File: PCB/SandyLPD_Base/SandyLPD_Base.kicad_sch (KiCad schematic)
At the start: 234 parts, among them J1 Conn_02x02_Odd_Even, J10 Conn_01x10_Pin, J11 Conn_01x03, J12 Conn_01x01_Pin, J2 Conn_01x03, J3 Conn_01x01_Pin, J4 Conn_01x10_Pin, J5 USB_C_Receptacle_USB2.0, J6 USB_C_Receptacle_USB2.0, J7 USB_C_Receptacle_USB2.0, J8 USB_C_Receptacle_USB2.0, J9 Conn_02x02_Odd_Even, SW1 BOOT_ALT, SW2 RESET_ALT, SW3 SW_DIP_x04, SW4 BOOT_ALT, SW5 RESET_ALT, SW6 SW_DIP_x04, U1 NCP1117-3.3_SOT223, U2 NCP1117-3.3_SOT223, U3 RP2040, U4 W25Q128JVPIQ, U5 RP2040, U6 W25Q128JVPIQ, Y1 12MHz, Y2 12MHz

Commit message: フラッシュメモリの部品置き換わりを修正
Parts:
- U4, U6: footprint Package_SO:SOIC-8_5.23x5.23mm_P1.27mm -> Package_SON:WSON-8-1EP_6x5mm_P1.27mm_EP3.4x4.3mm; symbol Memory_Flash:W25Q128JVS -> Memory_Flash:W25Q128JVP
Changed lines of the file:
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@@
 			)
 		)
-		(symbol "Memory_Flash:W25Q128JVS"
+		(symbol "Memory_Flash:W25Q128JVP"
 			(exclude_from_sim no)
 			(in_bom yes)
@@
 				)
 			)
-			(property "Value" "W25Q128JVS"
+			(property "Value" "W25Q128JVP"
 				(at 7.62 11.43 0)
 				(effects
@@
 				)
 			)
-			(property "Footprint" "Package_SO:SOIC-8_5.23x5.23mm_P1.27mm"
+			(property "Footprint" "Package_SON:WSON-8-1EP_6x5mm_P1.27mm_EP3.4x4.3mm"
 				(at 0 22.86 0)
 				(effects
@@
 				)
 			)
-			(property "Description" "128Mb Serial Flash Memory, Standard/Dual/Quad SPI, SOIC-8"
+			(property "Description" "128Mb Serial Flash Memory, Standard/Dual/Quad SPI, WSON-8"
 				(at 0 27.94 0)
 				(effects
@@
 				)
 			)
-			(property "ki_keywords" "flash memory SPI QPI DTR"
+			(property "ki_keywords" "flash memory SPI"
 				(at 0 0 0)
 				(effects
@@
 				)
 			)
-			(property "ki_fp_filters" "SOIC*5.23x5.23mm*P1.27mm*"
+			(property "ki_fp_filters" "WSON*1EP*6x5mm*P1.27mm*EP3.4x4.3mm*"
 				(at 0 0 0)
 				(effects
@@
 				)
 			)
-			(symbol "W25Q128JVS_0_1"
+			(symbol "W25Q128JVP_0_1"
 				(rectangle
 					(start -7.62 10.16)
@@
 				)
 			)
-			(symbol "W25Q128JVS_1_1"
+			(symbol "W25Q128JVP_1_1"
 				(pin input line
 					(at -10.16 7.62 0)
@@
 	)
 	(symbol
-		(lib_id "Memory_Flash:W25Q128JVS")
+		(lib_id "Memory_Flash:W25Q128JVP")
 		(at 305.435 144.78 0)
 		(unit 1)
@@
 			)
 		)
-		(property "Footprint" "Package_SO:SOIC-8_5.23x5.23mm_P1.27mm"
-			(at 305.435 144.78 0)
+		(property "Footprint" "Package_SON:WSON-8-1EP_6x5mm_P1.27mm_EP3.4x4.3mm"
+			(at 305.435 121.92 0)
 			(effects
 				(font
@@
 		)
 		(property "Datasheet" "https://www.winbond.com/resource-files/w25q128jv_dtr%20revc%2003272018%20plus.pdf"
-			(at 305.435 144.78 0)
+			(at 305.435 119.38 0)
 			(effects
 				(font
@@
 			)
 		)
-		(property "Description" "128Mb Serial Flash Memory, Standard/Dual/Quad SPI, SOIC-8"
-			(at 305.435 144.78 0)
+		(property "Description" "128Mb Serial Flash Memory, Standard/Dual/Quad SPI, WSON-8"
+			(at 305.435 116.84 0)
 			(effects
 				(font
@@
 	)
 	(symbol
-		(lib_id "Memory_Flash:W25Q128JVS")
+		(lib_id "Memory_Flash:W25Q128JVP")
 		(at 577.215 144.78 0)
 		(unit 1)
@@
 			)
 		)
-		(property "Footprint" "Package_SO:SOIC-8_5.23x5.23mm_P1.27mm"
-			(at 577.215 144.78 0)
+		(property "Footprint" "Package_SON:WSON-8-1EP_6x5mm_P1.27mm_EP3.4x4.3mm"
+			(at 577.215 121.92 0)
 			(effects
 				(font
@@
 		)
 		(property "Datasheet" "https://www.winbond.com/resource-files/w25q128jv_dtr%20revc%2003272018%20plus.pdf"
-			(at 577.215 144.78 0)
+			(at 577.215 119.38 0)
 			(effects
 				(font
@@
 			)
 		)
-		(property "Description" "128Mb Serial Flash Memory, Standard/Dual/Quad SPI, SOIC-8"
-			(at 577.215 144.78 0)
+		(property "Description" "128Mb Serial Flash Memory, Standard/Dual/Quad SPI, WSON-8"
+			(at 577.215 116.84 0)
 			(effects
 				(font

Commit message: 仮配線中
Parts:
- removed J3: Conn_01x01_Pin, TestPoint:TestPoint_THTPad_D1.0mm_Drill0.5mm, symbol Connector:Conn_01x01_Pin
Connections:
- net L_RESERVE1: now also J4.1 (Pin_1), U3.5 (GPIO3); no longer J4.3 (Pin_3), U3.4 (GPIO2)
- net L_RESERVE2: now also J4.2 (Pin_2), U3.6 (GPIO4); no longer J4.4 (Pin_4), U3.5 (GPIO3)
- net L_RESERVE3: now also J4.3 (Pin_3), U3.7 (GPIO5); no longer J4.5 (Pin_5), U3.6 (GPIO4)
- net L_RESERVE4: now also J4.4 (Pin_4), U3.8 (GPIO6); no longer J4.6 (Pin_6), U3.7 (GPIO5)
- net L_RESERVE5: now also J4.5 (Pin_5), U3.9 (GPIO7); no longer J4.7 (Pin_7), U3.8 (GPIO6)
- net L_RESERVE6: now also J4.7 (Pin_7), U3.11 (GPIO8); no longer J4.8 (Pin_8), U3.9 (GPIO7)
- net L_RESERVE7: now also J4.8 (Pin_8), U3.12 (GPIO9); no longer J4.9 (Pin_9), U3.11 (GPIO8)
- net L_RESERVE8: now also J4.9 (Pin_9), U3.13 (GPIO10); no longer J4.10 (Pin_10), U3.12 (GPIO9)
- net L_RESERVE9: now also J4.10 (Pin_10), U3.14 (GPIO11); no longer U3.13 (GPIO10)
- net L_col5: now also U3.4 (GPIO2); no longer U3.18 (GPIO15)
- net L_dip1: now also U3.15 (GPIO12); no longer U3.14 (GPIO11)
- net L_dip2: now also U3.16 (GPIO13); no longer U3.15 (GPIO12)
- net L_dip3: now also U3.17 (GPIO14); no longer U3.16 (GPIO13)
- net L_dip4: now also U3.18 (GPIO15); no longer U3.17 (GPIO14)
- no-connect marks 30 -> 29
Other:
- moved on the sheet: SW3, SW6

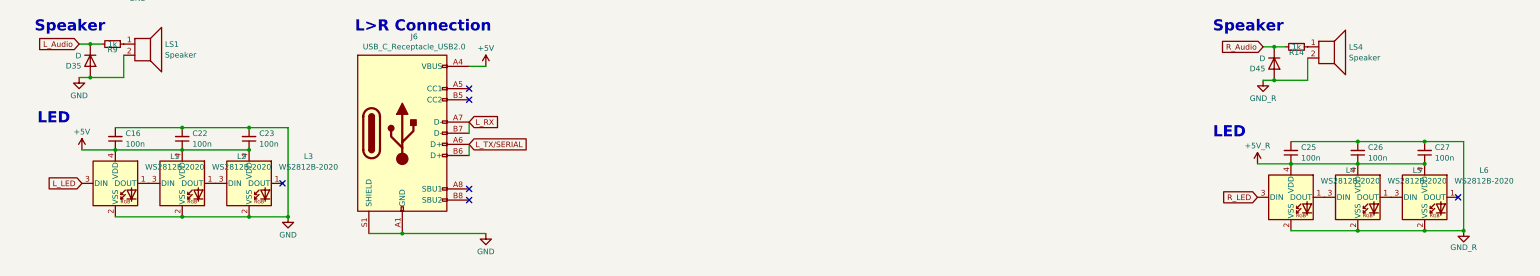
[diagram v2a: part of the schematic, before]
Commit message: LED、WS2812Cはパスコン不要のため、仮想パーツとして実際には配置しない。
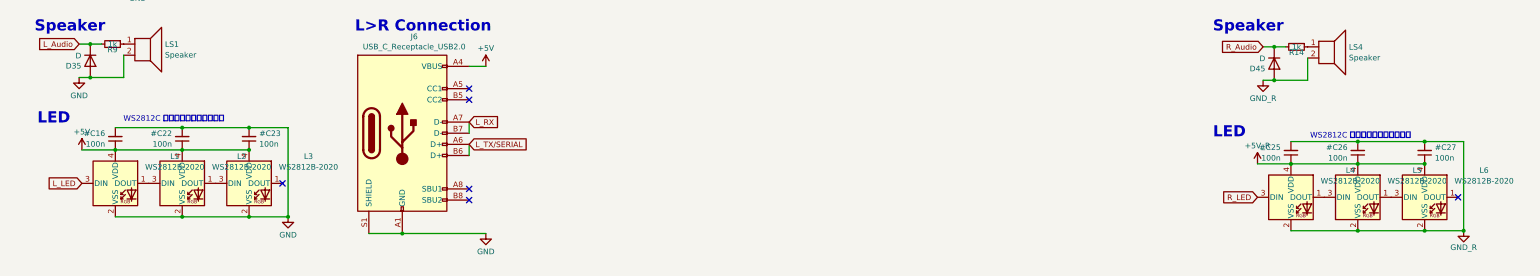
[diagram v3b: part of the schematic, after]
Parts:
- renumbered C16 to #C16, C22 to #C22, C23 to #C23, C25 to #C25, C26 to #C26, C27 to #C27
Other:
- note added: "WS2812C バイパスコンデンサ不要"
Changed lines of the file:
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@@
 		)
 	)
+	(text "WS2812C バイパスコンデンサ不要"
+		(exclude_from_sim no)
+		(at 376.555 210.82 0)
+		(effects
+			(font
+				(size 1.27 1.27)
+			)
+		)
+	)
 	(text "SCREWS to Mid"
 		(exclude_from_sim no)
@@
 		)
 	)
+	(text "WS2812C バイパスコンデンサ不要"
+		(exclude_from_sim no)
+		(at 647.065 214.63 0)
+		(effects
+			(font
+				(size 1.27 1.27)
+			)
+		)
+	)
 	(text "Base to Mid Left"
 		(exclude_from_sim no)
@@
 		(on_board yes)
 		(dnp no)
-		(property "Reference" "C23"
+		(property "Reference" "#C23"
 			(at 396.0241 214.0464 0)
 			(effects
@@
 			(project "SandyLPD_Base"
 				(path "/a99ab643-cdc7-4f8c-8088-c1f4faa914d1"
-					(reference "C23")
+					(reference "#C23")
 					(unit 1)
 				)
@@
 		(dnp no)
 		(fields_autoplaced yes)
-		(property "Reference" "C16"
-			(at 365.5441 214.0464 0)
+		(property "Reference" "#C16"
+			(at 360.8959 214.0464 0)
 			(effects
 				(font
 					(size 1.27 1.27)
 				)
-				(justify right)
+				(justify left)
 			)
 		)
 		(property "Value" "100n"
-			(at 365.5441 216.4707 0)
+			(at 360.8959 216.4707 0)
 			(effects
 				(font
 					(size 1.27 1.27)
 				)
-				(justify right)
+				(justify left)
 			)
 		)
@@
 			(project "SandyLP_Base"
 				(path "/a99ab643-cdc7-4f8c-8088-c1f4faa914d1"
-					(reference "C16")
+					(reference "#C16")
 					(unit 1)
 				)
@@
 		(on_board yes)
 		(dnp no)
-		(property "Reference" "C27"
+		(property "Reference" "#C27"
 			(at 663.9941 217.2214 0)
 			(effects
@@
 			(project "SandyLPD_Base"
 				(path "/a99ab643-cdc7-4f8c-8088-c1f4faa914d1"
-					(reference "C27")
+					(reference "#C27")
 					(unit 1)
 				)
@@
 		(dnp no)
 		(fields_autoplaced yes)
-		(property "Reference" "C25"
-			(at 633.5141 217.2214 0)
+		(property "Reference" "#C25"
+			(at 628.8659 217.2214 0)
 			(effects
 				(font
 					(size 1.27 1.27)
 				)
-				(justify right)
+				(justify left)
 			)
 		)
 		(property "Value" "100n"
-			(at 633.5141 219.6457 0)
+			(at 628.8659 219.6457 0)
 			(effects
 				(font
 					(size 1.27 1.27)
 				)
-				(justify right)
+				(justify left)
 			)
 		)
@@
 			(project "SandyLPD_Base"
 				(path "/a99ab643-cdc7-4f8c-8088-c1f4faa914d1"
-					(reference "C25")
+					(reference "#C25")
 					(unit 1)
 				)
@@
 		(dnp no)
 		(fields_autoplaced yes)
-		(property "Reference" "C26"
-			(at 648.7541 217.2214 0)
+		(property "Reference" "#C26"
+			(at 644.1059 217.2214 0)
 			(effects
 				(font
 					(size 1.27 1.27)
 				)
-				(justify right)
+				(justify left)
 			)
 		)
 		(property "Value" "100n"
-			(at 648.7541 219.6457 0)
+			(at 644.1059 219.6457 0)
 			(effects
 				(font
 					(size 1.27 1.27)
 				)
-				(justify right)
+				(justify left)
 			)
 		)
@@
 			(project "SandyLPD_Base"
 				(path "/a99ab643-cdc7-4f8c-8088-c1f4faa914d1"
-					(reference "C26")
+					(reference "#C26")
 					(unit 1)
 				)
@@
 		(dnp no)
 		(fields_autoplaced yes)
-		(property "Reference" "C22"
-			(at 380.7841 214.0464 0)
+		(property "Reference" "#C22"
+			(at 376.1359 214.0464 0)
 			(effects
 				(font
 					(size 1.27 1.27)
 				)
-				(justify right)
+				(justify left)
 			)
 		)
 		(property "Value" "100n"
-			(at 380.7841 216.4707 0)
+			(at 376.1359 216.4707 0)
 			(effects
 				(font
 					(size 1.27 1.27)
 				)
-				(justify right)
+				(justify left)
 			)
 		)
@@
 			(project "SandyLPD_Base"
 				(path "/a99ab643-cdc7-4f8c-8088-c1f4faa914d1"
-					(reference "C22")
+					(reference "#C22")
 					(unit 1)
 				)

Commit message: パーツ配置調整中
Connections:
- net GND_R: now also H_mid_13.1; no longer H_mid_14.1
- net L_col0: now also H_mid_8.1, U3.35 (GPIO23); no longer H_mid_2.1, U3.39 (GPIO27_ADC1)
- net L_col1: now also H_mid_2.1, U3.36 (GPIO24); no longer H_mid_8.1, U3.38 (GPIO26_ADC0)
- net L_col3: now also U3.38 (GPIO26_ADC0); no longer U3.36 (GPIO24)
- net L_col4: now also U3.40 (GPIO28_ADC2); no longer U3.35 (GPIO23)
- net L_row0: now also U3.39 (GPIO27_ADC1); no longer U3.40 (GPIO28_ADC2)
- net R_col0: now also H_mid_14.1; no longer H_mid_13.1
- net R_col1: now also H_mid_6.1; no longer H_mid_7.1
- net R_row0: now also H_mid_7.1; no longer H_mid_6.1
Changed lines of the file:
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@@
 	(global_label "L_col4"
 		(shape input)
-		(at 393.7 153.67 0)
+		(at 393.7 168.91 0)
 		(fields_autoplaced yes)
 		(effects
@@
 		)
 		(property "Intersheetrefs" "${INTERSHEET_REFS}"
-			(at 402.139 153.67 0)
+			(at 402.139 168.91 0)
 			(effects
 				(font
@@
 		)
 		(property "シート間のリファレンス" "${INTERSHEET_REFS}"
-			(at 393.7 155.5052 0)
+			(at 393.7 170.7452 0)
 			(effects
 				(font
@@
 	(global_label "R_row0"
 		(shape input)
-		(at 399.415 314.325 180)
+		(at 422.275 314.325 180)
 		(fields_autoplaced yes)
 		(effects
@@
 		)
 		(property "Intersheetrefs" "${INTERSHEET_REFS}"
-			(at 390.3712 314.325 0)
+			(at 413.2312 314.325 0)
 			(effects
 				(font
@@
 		)
 		(property "シート間のリファレンス" "${INTERSHEET_REFS}"
-			(at 399.415 316.1602 0)
+			(at 422.275 316.1602 0)
 			(effects
 				(font
@@
 	(global_label "L_row0"
 		(shape input)
-		(at 393.7 168.91 0)
+		(at 393.7 166.37 0)
 		(fields_autoplaced yes)
 		(effects
@@
 		)
 		(property "Intersheetrefs" "${INTERSHEET_REFS}"
-			(at 402.5019 168.91 0)
+			(at 402.5019 166.37 0)
 			(effects
 				(font
@@
 		)
 		(property "シート間のリファレンス" "${INTERSHEET_REFS}"
-			(at 393.7 170.7452 0)
+			(at 393.7 168.2052 0)
 			(effects
 				(font
@@
 	(global_label "L_col0"
 		(shape input)
-		(at 393.7 166.37 0)
+		(at 393.7 153.67 0)
 		(fields_autoplaced yes)
 		(effects
@@
 		)
 		(property "Intersheetrefs" "${INTERSHEET_REFS}"
-			(at 402.139 166.37 0)
+			(at 402.139 153.67 0)
 			(effects
 				(font
@@
 		)
 		(property "シート間のリファレンス" "${INTERSHEET_REFS}"
-			(at 393.7 168.2052 0)
+			(at 393.7 155.5052 0)
 			(effects
 				(font
@@
 	(global_label "L_col3"
 		(shape input)
-		(at 393.7 156.21 0)
+		(at 393.7 163.83 0)
 		(fields_autoplaced yes)
 		(effects
@@
 		)
 		(property "Intersheetrefs" "${INTERSHEET_REFS}"
-			(at 402.139 156.21 0)
+			(at 402.139 163.83 0)
 			(effects
 				(font
@@
 		)
 		(property "シート間のリファレンス" "${INTERSHEET_REFS}"
-			(at 393.7 158.0452 0)
+			(at 393.7 165.6652 0)
 			(effects
 				(font
@@
 	(global_label "L_col1"
 		(shape input)
-		(at 393.7 163.83 0)
+		(at 393.7 156.21 0)
 		(fields_autoplaced yes)
 		(effects
@@
 		)
 		(property "Intersheetrefs" "${INTERSHEET_REFS}"
-			(at 402.139 163.83 0)
+			(at 402.139 156.21 0)
 			(effects
 				(font
@@
 		)
 		(property "シート間のリファレンス" "${INTERSHEET_REFS}"
-			(at 393.7 165.6652 0)
+			(at 393.7 158.0452 0)
 			(effects
 				(font
@@
 	(global_label "R_col1"
 		(shape input)
-		(at 422.275 314.325 180)
+		(at 399.415 314.325 180)
 		(fields_autoplaced yes)
 		(effects
@@
 		)
 		(property "Intersheetrefs" "${INTERSHEET_REFS}"
-			(at 413.5941 314.325 0)
+			(at 390.7341 314.325 0)
 			(effects
 				(font
@@
 		)
 		(property "シート間のリファレンス" "${INTERSHEET_REFS}"
-			(at 422.275 316.1602 0)
+			(at 399.415 316.1602 0)
 			(effects
 				(font
@@
 	(global_label "L_col1"
 		(shape input)
-		(at 196.215 324.485 180)
+		(at 219.075 314.325 180)
 		(fields_autoplaced yes)
 		(effects
@@
 		)
 		(property "Intersheetrefs" "${INTERSHEET_REFS}"
-			(at 187.776 324.485 0)
+			(at 210.636 314.325 0)
 			(effects
 				(font
@@
 		)
 		(property "シート間のリファレンス" "${INTERSHEET_REFS}"
-			(at 196.215 326.3202 0)
+			(at 219.075 316.1602 0)
 			(effects
 				(font
@@
 	(global_label "R_col0"
 		(shape input)
-		(at 399.415 324.485 180)
+		(at 422.275 324.485 180)
 		(fields_autoplaced yes)
 		(effects
@@
 		)
 		(property "Intersheetrefs" "${INTERSHEET_REFS}"
-			(at 390.7341 324.485 0)
+			(at 413.5941 324.485 0)
 			(effects
 				(font
@@
 		)
 		(property "シート間のリファレンス" "${INTERSHEET_REFS}"
-			(at 399.415 326.3202 0)
+			(at 422.275 326.3202 0)
 			(effects
 				(font
@@
 	(global_label "L_col0"
 		(shape input)
-		(at 219.075 314.325 180)
+		(at 196.215 324.485 180)
 		(fields_autoplaced yes)
 		(effects
@@
 		)
 		(property "Intersheetrefs" "${INTERSHEET_REFS}"
-			(at 210.636 314.325 0)
+			(at 187.776 324.485 0)
 			(effects
 				(font
@@
 		)
 		(property "シート間のリファレンス" "${INTERSHEET_REFS}"
-			(at 219.075 316.1602 0)
+			(at 196.215 326.3202 0)
 			(effects
 				(font
@@
 			)
 		)
-		(property "Datasheet" "~"
+		(property "Datasheet" "https://akizukidenshi.com/catalog/g/g108275/"
 			(at 367.03 29.845 90)
 			(effects
@@
 	(symbol
 		(lib_id "power:GND")
-		(at 422.275 324.485 0)
+		(at 399.415 324.485 0)
 		(unit 1)
 		(exclude_from_sim no)
@@
 		(fields_autoplaced yes)
 		(property "Reference" "#PWR060"
-			(at 422.275 330.835 0)
+			(at 399.415 330.835 0)
 			(effects
 				(font
@@
 		)
 		(property "Value" "GND_R"
-			(at 422.275 328.6181 0)
+			(at 399.415 328.6181 0)
 			(effects
 				(font
@@
 		)
 		(property "Footprint" ""
-			(at 422.275 324.485 0)
+			(at 399.415 324.485 0)
 			(effects
 				(font
@@
 		)
 		(property "Datasheet" ""
-			(at 422.275 324.485 0)
+			(at 399.415 324.485 0)
 			(effects
 				(font
@@
 		)
 		(property "Description" "Power symbol creates a global label with name \"GND\" , ground"
-			(at 422.275 324.485 0)
+			(at 399.415 324.485 0)
 			(effects
 				(font

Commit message: 左手のパーツ配置と配線、一旦完了。
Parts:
- removed J12: Conn_01x01_Pin, TestPoint:TestPoint_THTPad_D1.0mm_Drill0.5mm, symbol Connector:Conn_01x01_Pin
- renumbered T_L_C1 to T_L_C0, T_L_C2 to T_L_C1, T_L_C3 to T_L_C2, T_L_C4 to T_L_C3, T_L_C5 to T_L_C4, T_L_C6 to T_L_C5, T_L_R1 to T_L_R0, T_L_R2 to T_L_R1, T_L_R3 to T_L_R2, T_L_R4 to T_L_R3, T_R_C6 to T_R_C0, T_R_C5 to T_R_C1, T_R_C4 to T_R_C2, T_R_C2 to T_R_C4, T_R_C1 to T_R_C5, T_R_R1 to T_R_R0, T_R_R2 to T_R_R1, T_R_R3 to T_R_R2, T_L_R5 to T_R_R3
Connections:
- net GND: now also J4.6 (Pin_6); no longer C19.2, C20.2, SW_26.C
- net GND_R: now also C19.2, C20.2, J10.6 (Pin_6), SW_26.C
- net R_GPIO12: now also J10.7 (Pin_7)
- net R_GPIO22: now also J10.1 (Pin_1); no longer J10.3 (Pin_3)
- net R_GPIO23: now also J10.2 (Pin_2); no longer J10.4 (Pin_4)
- net R_GPIO24: now also J10.3 (Pin_3); no longer J10.5 (Pin_5)
- net R_GPIO25: now also J10.4 (Pin_4); no longer J10.6 (Pin_6)
- net R_GPIO26: now also J10.5 (Pin_5); no longer J10.7 (Pin_7)
- no-connect marks 29 -> 26

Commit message: 右手MCUまわりの配置中
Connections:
- net R_GPIO12 renamed R_RESERVE1
- net R_RESERVE1: now also J10.1 (Pin_1); no longer J10.7 (Pin_7)
- net R_GPIO22 renamed R_RESERVE2
- net R_RESERVE2: now also J10.2 (Pin_2); no longer J10.1 (Pin_1)
- net R_GPIO23 renamed R_RESERVE3
- net R_RESERVE3: now also J10.3 (Pin_3); no longer J10.2 (Pin_2)
- net R_GPIO24 renamed R_RESERVE4
- net R_RESERVE4: now also J10.4 (Pin_4); no longer J10.3 (Pin_3)
- net R_GPIO25 renamed R_RESERVE5
- net R_RESERVE5: now also J10.5 (Pin_5); no longer J10.4 (Pin_4)
- net R_GPIO26 renamed R_RESERVE6
- net R_RESERVE6: now also J10.7 (Pin_7); no longer J10.5 (Pin_5)
- net R_GPIO27 renamed R_RESERVE7
- net R_GPIO28 renamed R_RESERVE8
- net R_GPIO29 renamed R_RESERVE9
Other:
- moved on the sheet: J10, R17, R18, R22, U5

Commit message: EC11Kサポート廃止（新規設計非推奨のため）
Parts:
- SW_25, SW_26: footprint locallib:ChocV2_AND_RotaryEncoder_Alps_EC11K-Switch_Vertical_H20mm_NPTH_MP_minimal -> locallib:ChocV2_AND_RotaryEncoder_Alps_EC11E-Switch_Vertical_H20mm_NPTH_MP_minimal
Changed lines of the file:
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@@
 			)
 		)
-		(property "Footprint" "locallib:ChocV2_AND_RotaryEncoder_Alps_EC11K-Switch_Vertical_H20mm_NPTH_MP_minimal"
+		(property "Footprint" "locallib:ChocV2_AND_RotaryEncoder_Alps_EC11E-Switch_Vertical_H20mm_NPTH_MP_minimal"
 			(at 52.07 105.791 0)
 			(effects
@@
 			)
 		)
-		(property "Footprint" "locallib:ChocV2_AND_RotaryEncoder_Alps_EC11K-Switch_Vertical_H20mm_NPTH_MP_minimal"
+		(property "Footprint" "locallib:ChocV2_AND_RotaryEncoder_Alps_EC11E-Switch_Vertical_H20mm_NPTH_MP_minimal"
 			(at 243.84 105.791 0)
 			(effects
